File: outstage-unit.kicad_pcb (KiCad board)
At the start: 2 copper layers, 100 x 220 mm, 76 parts, among them J101 Conn_01x06_Socket, M101 Fan, Q201 DNLS350E, Q202 DPLS350E, Q203 TIP41C, Q204 TIP42C, Q301 DNLS350E, Q302 DPLS350E, Q303 TIP41C, Q304 TIP42C, Q401 DNLS350E, Q402 DPLS350E, Q403 TIP41C, Q404 TIP42C, Q501 DNLS350E, Q502 DPLS350E, Q503 TIP41C, Q504 TIP42C, Q601 DNLS350E, Q602 DPLS350E, Q603 TIP41C, Q604 TIP42C, Q701 DNLS350E, Q702 DPLS350E, Q703 TIP41C, Q704 TIP42C

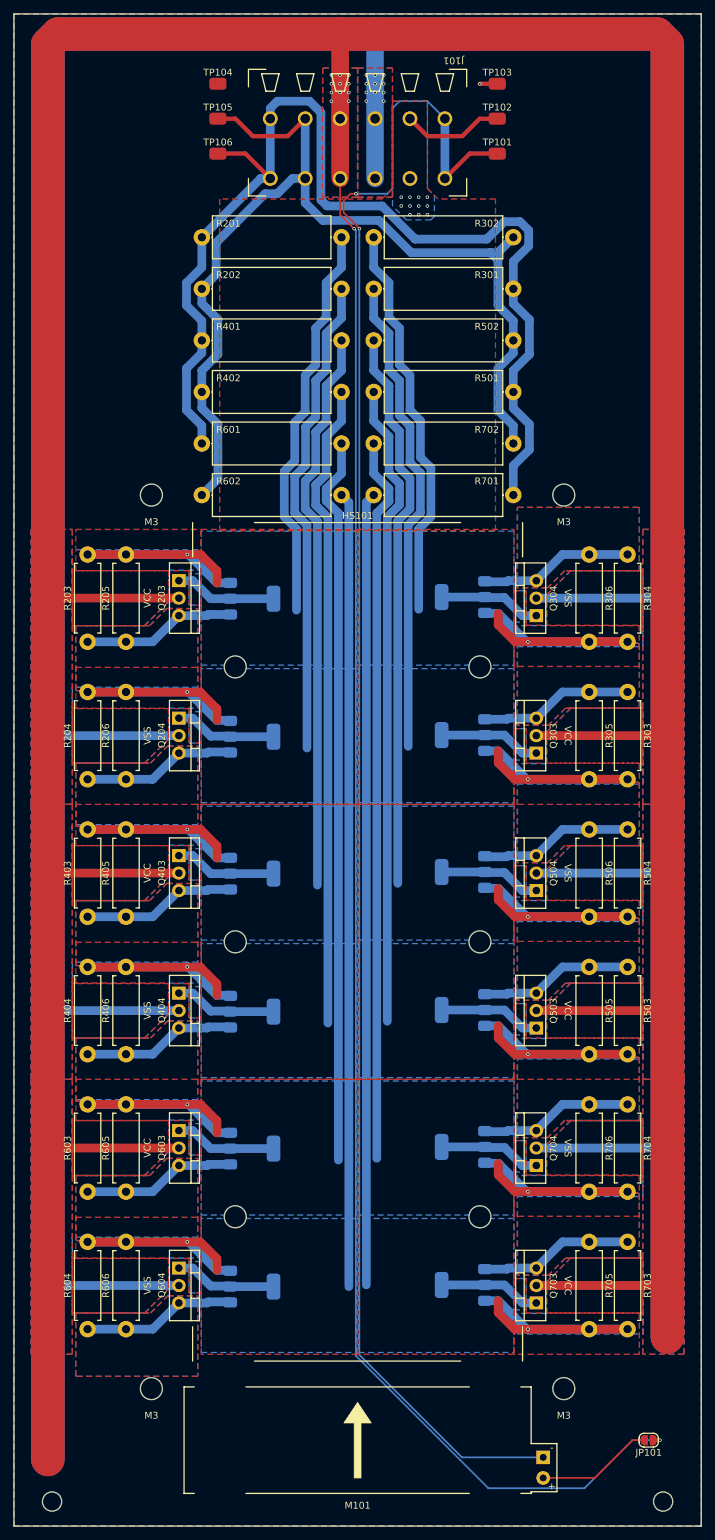
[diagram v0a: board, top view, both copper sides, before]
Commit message: add pcb outstage-unit silkscreen notes
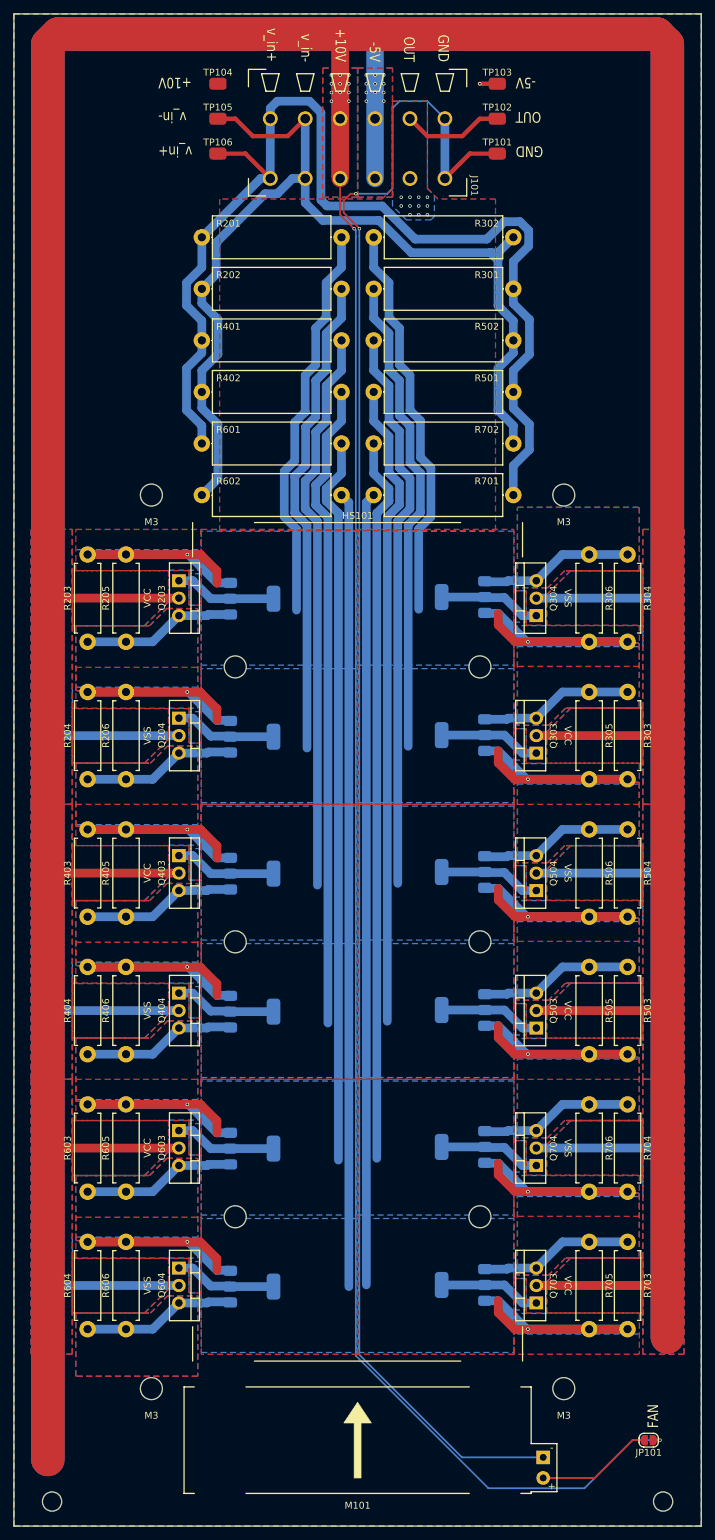
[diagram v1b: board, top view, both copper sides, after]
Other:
- board text added: "FAN"
- board text added: "GND OUT -5V"
- board text added: "GND OUT -5V +10V v_in- v_in+"
- board text added: "v_in+ v_in- +10V"
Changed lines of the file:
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@@
 		(at 97.7 43.94 180)
 		(property "Reference" "J101"
-			(at -1.27 17.145 180)
+			(at -4.3 -1.06 -90)
 			(unlocked yes)
 			(layer "F.SilkS")
@@
 		)
 	)
+	(gr_text "FAN"
+		(at 128 224 90)
+		(layer "F.SilkS")
+		(effects
+			(font
+				(size 1.5494 1.27)
+				(thickness 0.15)
+			)
+		)
+	)
 	(gr_text "VCC"
 		(at 55 145 90)
@@
 		)
 	)
+	(gr_text "GND\n\nOUT\n\n-5V\n\n+10V\n\nv_in-\n\nv_in+"
+		(at 85 27 270)
+		(layer "F.SilkS")
+		(effects
+			(font
+				(size 1.5494 1.27)
+				(thickness 0.15)
+			)
+			(justify right)
+		)
+	)
 	(gr_text "VSS"
 		(at 55 205 90)
@@
 		)
 	)
+	(gr_text "v_in+\n\nv_in-\n\n+10V"
+		(at 56 35 180)
+		(layer "F.SilkS")
+		(effects
+			(font
+				(size 1.5494 1.27)
+				(thickness 0.15)
+			)
+			(justify right)
+		)
+	)
 	(gr_text "VCC"
 		(at 115 165 -90)
@@
 		)
 	)
+	(gr_text "GND\n\nOUT\n\n-5V"
+		(at 108 35 180)
+		(layer "F.SilkS")
+		(effects
+			(font
+				(size 1.5494 1.27)
+				(thickness 0.15)
+			)
+			(justify right)
+		)
+	)
 	(gr_text "VSS"
 		(at 115 105 -90)
@@
 		)
 		(height -8.57)
-		(gr_text "88.9000 mm"
+		(gr_text "3500.0000 mils"
 			(locked yes)
 			(at 85 243.85 0)
@@
 		(height -5)
 		(orientation 1)
-		(gr_text "3.5700 mm"
+		(gr_text "140.5512 mils"
 			(locked yes)
 			(at 28 238 90)
